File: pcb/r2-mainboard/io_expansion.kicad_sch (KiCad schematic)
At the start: 16 parts, among them J22 HC-FPC-05-09-6RLTAG, J23 HC-FPC-05-09-6RLTAG, J28 USB-C 16P, U54 TPS22914BYFPR, U55 TPS22914BYFPR, U56 TPS2553DBVR, U57 USBLC6-2SC6

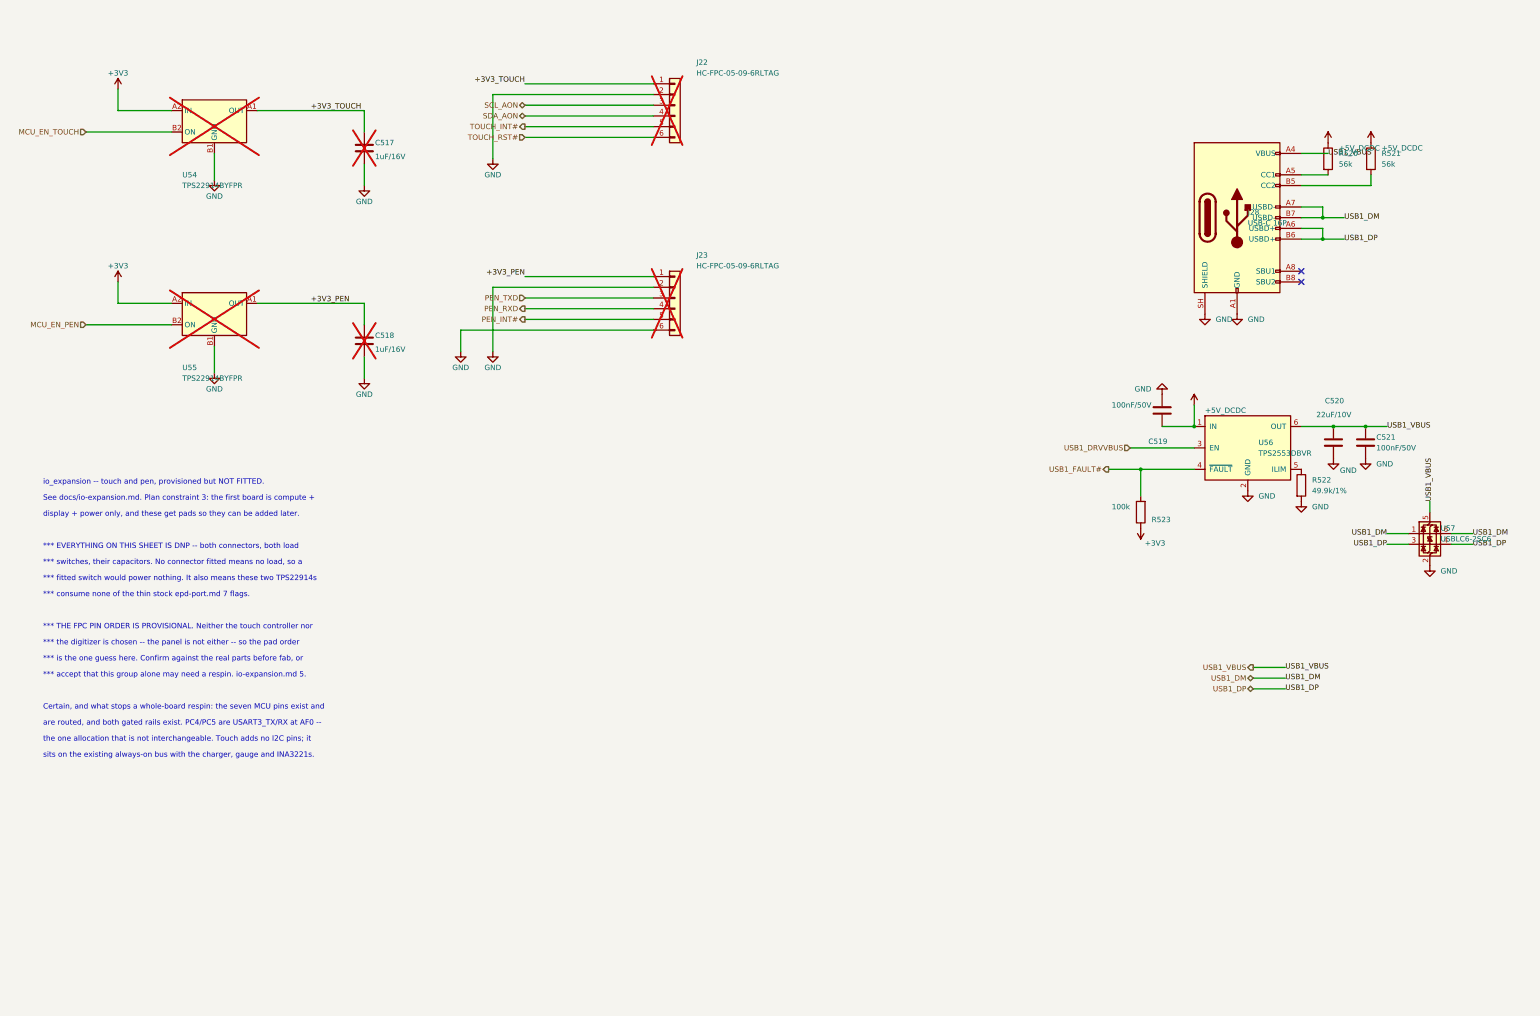
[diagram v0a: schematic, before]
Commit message: Touch decided: I2C hand-wired for the prototype; Caster bitgen applied
Good Display's answer of 2026-08-31 closes the on-board GT9110H idea:
the driving board is another customer's design and they will not share
files, so the panel's ITO channel map is unobtainable at prototype
scale. The production path is now priced instead -- US$750 tooling,
MOQ 1000/lot, for a custom panel with the interface and touch IC of our
choosing.

Owner's decision: option C. Touch runs over I2C on J22, hand-wired to
the vendor board's test points for the prototype. USB was rejected --
USB0 is the charge port and USB1 is now the host port, so USB touch
would have needed a hub and would have cost touch-to-wake permanently.
No schematic change: J22/J23 and U54/U55 stay exactly as drawn, DNP.

io-expansion.md 5.2 records the decision and the three firmware ways to
disable touch-to-wake; 5.3 records a real gap found on the vendor board
-- it exposes SDA/SCL/VDD/GND/DBG/INT/DP and *no* RST pad, so reset
becomes a power cycle through MCU_EN_TOUCH, and the GT9110's I2C
address cannot be selected and must be scanned for at bring-up.

Also in this commit, the owner's work: Caster bitgen at ConfigRate 22 /
x4 / binary (submodule pointer bump), epd_power and io_expansion sheet
edits, and board layout.

Co-Authored-By: Claude Opus 5 <noreply@anthropic.com>
Claude-Session: https://claude.ai/code/session_01MHTAe6ZnhogTEgtyPcLhwG
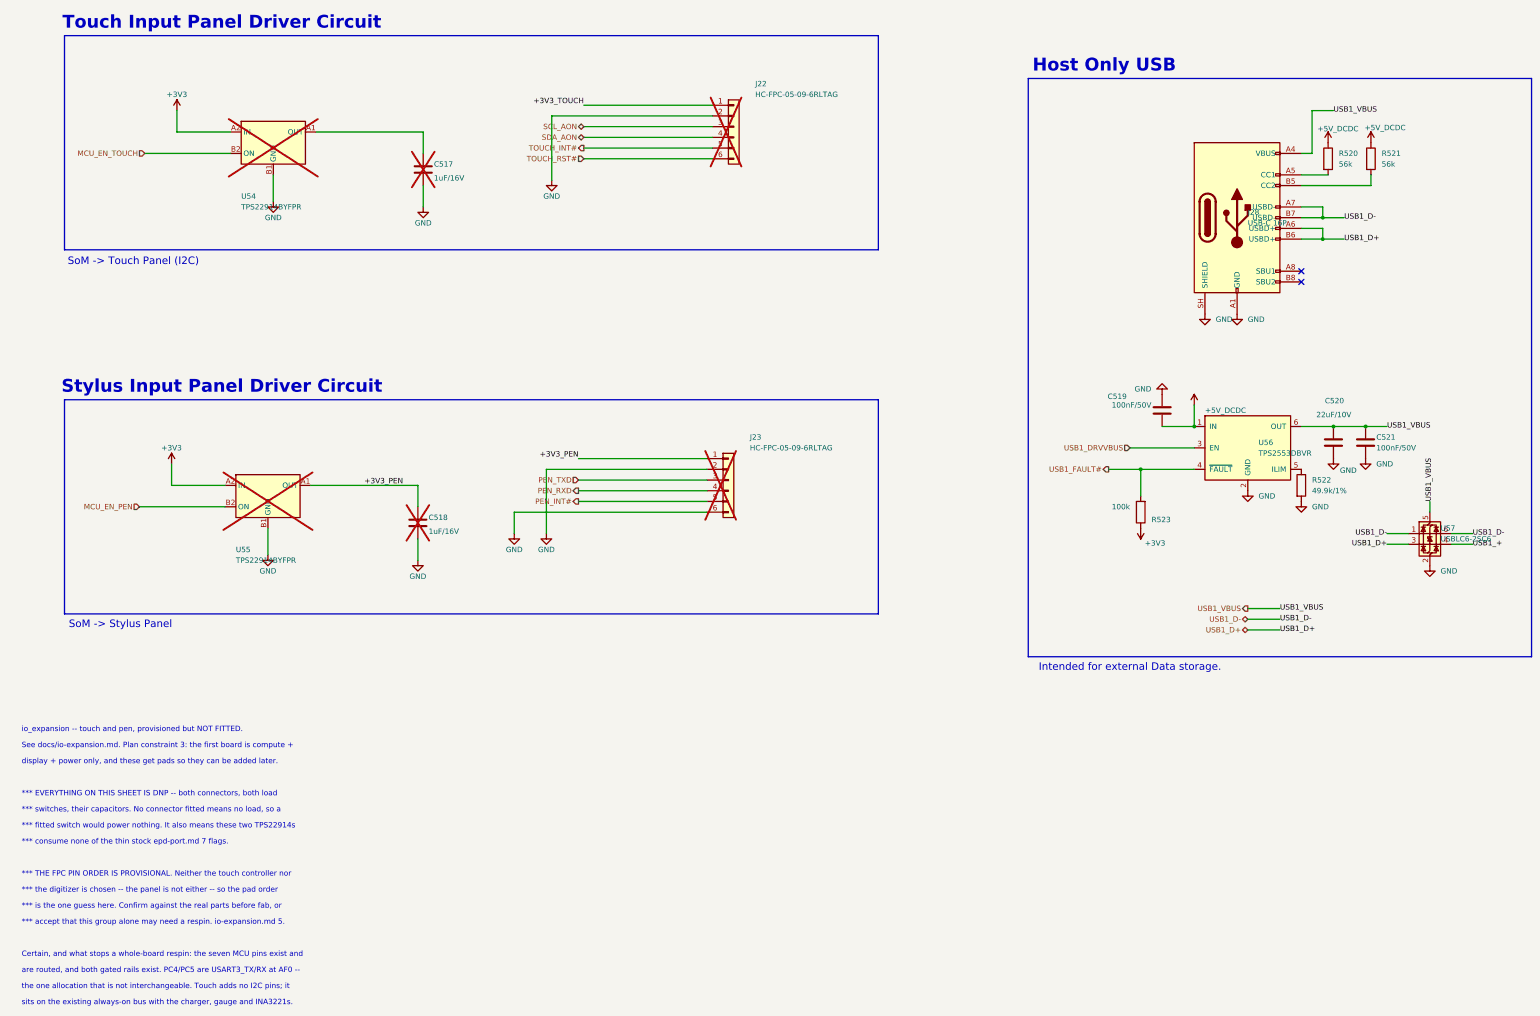
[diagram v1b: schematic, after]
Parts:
- C518, J23, U55: now left out of the parts list
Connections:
- net +3V3_TOUCH: no longer C517.1, U54.A1 (OUT)
- net USB1_DM renamed USB1_D-
- net USB1_DP renamed USB1_D+
- net USB1_D+: no longer U57.4 (I/O2)
- new net: C517.1, U54.A1 (OUT)
- new net USB1_+: U57.4 (I/O2)
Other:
- note added: "Host Only USB"
- note added: "Intended for external Data storage."
- note added: "SoM -> Stylus Panel"
- note added: "SoM -> Touch Panel (I2C)"
- note added: "Stylus Input Panel Driver Circuit"
- note added: "Touch Input Panel Driver Circuit"
- moved on the sheet: C517, C518, J22, J23, U54, U55

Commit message: Docs: library audit list and a first production costing
libraries.md -- every symbol in r2.kicad_sym and every footprint in
r2.pretty, with what it was derived from, which tools/ script emits it,
and what was actually checked. Written for the owner's audit before the
libraries get rehomed. Notes that pcb_common has never been modified,
and calls out the three newest entries (TPS2553DBV and the two
_Mirrored FPC land patterns) as the least reviewed.

NOTES-production-costing.md -- what 1000 units costs and what a campaign
would have to raise, prompted by Good Display's US$750 / MOQ 1000 quote.
Central estimate EUR 340/unit COGS and a EUR ~548k goal, but the honest
finding is the sensitivity: the PCM-071 at EUR 250 @1-9 costs more than
the display, and the sibling quote says ~EUR 190 of that is a memory-
shortage surcharge. A 1000-piece quote moves the goal by EUR 290k, so it
is the single highest-value thing to chase. Also states plainly that at
the central estimate the margin is thin to negative against market
comparables, and what to do about it.

Both indexed in CLAUDE.md.

Co-Authored-By: Claude Opus 5 <noreply@anthropic.com>
Claude-Session: https://claude.ai/code/session_01MHTAe6ZnhogTEgtyPcLhwG
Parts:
- C517, J22, U54: now fitted
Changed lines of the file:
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@@
 	(wire
 		(pts
-			(xy 69.85 73.66) (xy 49.53 73.66)
+			(xy 69.85 73.66) (xy 54.61 73.66)
 		)
 		(stroke
@@
 	(wire
 		(pts
-			(xy 146.05 64.77) (xy 146.05 80.01)
+			(xy 137.16 64.77) (xy 137.16 77.47)
 		)
 		(stroke
@@
 	(wire
 		(pts
-			(xy 184.15 64.77) (xy 146.05 64.77)
+			(xy 184.15 64.77) (xy 137.16 64.77)
 		)
 		(stroke
@@
 	(hierarchical_label "MCU_EN_TOUCH"
 		(shape input)
-		(at 49.53 73.66 180)
+		(at 54.61 73.66 180)
 		(effects
 			(font
@@
 	(symbol
 		(lib_id "power:GND")
-		(at 146.05 80.01 0)
+		(at 137.16 77.47 0)
 		(unit 1)
 		(body_style 1)
@@
 		(dnp no)
 		(property "Reference" "#PWR1107"
-			(at 146.05 80.01 0)
+			(at 137.16 77.47 0)
 			(hide yes)
 			(show_name no)
@@
 		)
 		(property "Value" "GND"
-			(at 146.05 83.82 0)
+			(at 137.16 81.28 0)
 			(show_name no)
 			(do_not_autoplace no)
@@
 		)
 		(property "Footprint" ""
-			(at 146.05 80.01 0)
+			(at 137.16 77.47 0)
 			(hide yes)
 			(show_name no)
@@
 		)
 		(property "Datasheet" ""
-			(at 146.05 80.01 0)
+			(at 137.16 77.47 0)
 			(hide yes)
 			(show_name no)
@@
 		)
 		(property "Description" ""
-			(at 146.05 80.01 0)
+			(at 137.16 77.47 0)
 			(hide yes)
 			(show_name no)
@@
 		(on_board yes)
 		(in_pos_files yes)
-		(dnp yes)
+		(dnp no)
 		(property "Reference" "C517"
 			(at 118.11 76.2 0)
@@
 		(on_board yes)
 		(in_pos_files yes)
-		(dnp yes)
+		(dnp no)
 		(property "Reference" "J22"
 			(at 194.31 57.15 0)
@@
 		(on_board yes)
 		(in_pos_files yes)
-		(dnp yes)
+		(dnp no)
 		(property "Reference" "U54"
-			(at 72.39 83.82 0)
+			(at 77.724 61.976 0)
 			(show_name no)
 			(do_not_autoplace no)
@@
 		)
 		(property "Value" "TPS22914BYFPR"
-			(at 72.39 86.36 0)
-			(show_name no)
-			(do_not_autoplace no)
+			(at 77.724 64.516 0)
+			(show_name no)
+			(do_not_autoplace no)

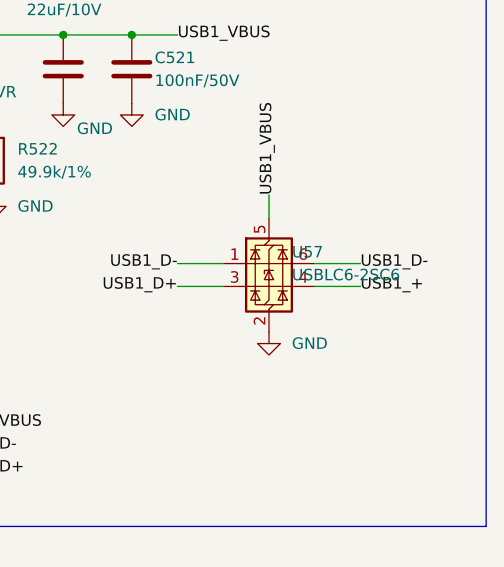
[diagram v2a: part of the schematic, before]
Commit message: Recover from the KiCad crash; finish the USB1_D+/D- rename
KiCad crashed and deleted 150 tracked files plus 19 untracked ones.
Recovery, in the order that matters:

  1. copied _restore_backup_2026-08-31T20-57-08-688 aside (261 MB)
  2. rescued the 4 untracked files that existed only there -- the
     PHYTEC PCM-071 STEP/x_t/Basic models and the library/3dmodels copy.
     The other 15 were __pycache__, .lck and .bak.
  3. git checkout of the 150 deletions (deletions only, so the six
     modified files were never touched)
  4. three files the crash had *rolled back* rather than deleted, and
     which git checkout therefore missed, restored from HEAD:
       r2.kicad_sym    -- was 11 symbols, missing TPS2553DBV,
                          BTH-060_AB/CD and BOM_ITEM, and carrying the
                          superseded PCM-071 symbol: the pre-2026-08-20
                          state, before the SoM was split in two
       sym-lib-table   -- had lost the Reflow declaration
       fp-lib-table    -- had lost Reflow and (version 7)

r2.kicad_pcb was not damaged -- 328 footprints, 471 segments, same as
HEAD. Rescuing PCM-071_1573-1.STEP also repairs X2's 3D model path,
which an earlier restore had broken.

Separately, the USB1 net rename is finished at the owner's request:
som.kicad_sch USB1_DM/DP -> USB1_D-/D+ (the J26 X_USB1_* pin names are
PHYTEC's and are untouched), and a USB1_+ typo on U57's second ESD stub
in io_expansion corrected to USB1_D+. sheet_pins + wire_root re-run:
113 names on 233 sheet pins, 113 joined, 0 one-sided. All five USB1
nets verified node-for-node.

⚠ The tree is mid-renumber (J200/U200/U300... appearing) and carries one
severed net: +3V3_TOUCH reaches only J22.1, while U54.A1 and C517.1 sit
on an unnamed Net-(U54-OUT). Committed as-is so the recovery is not at
risk from another crash; the break is called out rather than hidden.

Co-Authored-By: Claude Opus 5 <noreply@anthropic.com>
Claude-Session: https://claude.ai/code/session_01MHTAe6Znh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
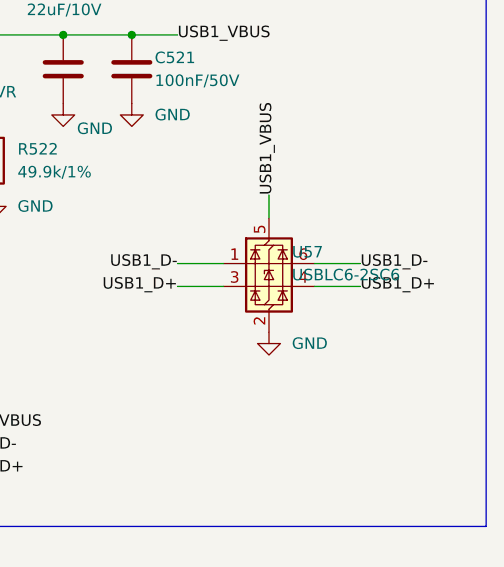
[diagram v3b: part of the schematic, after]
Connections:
- net USB1_+ is gone; now on net USB1_D+: U57.4 (I/O2)
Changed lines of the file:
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@@
 		)
 	)
-	(label "USB1_+"
+	(label "USB1_D+"
 		(at 364.49 166.37 0)
 		(effects

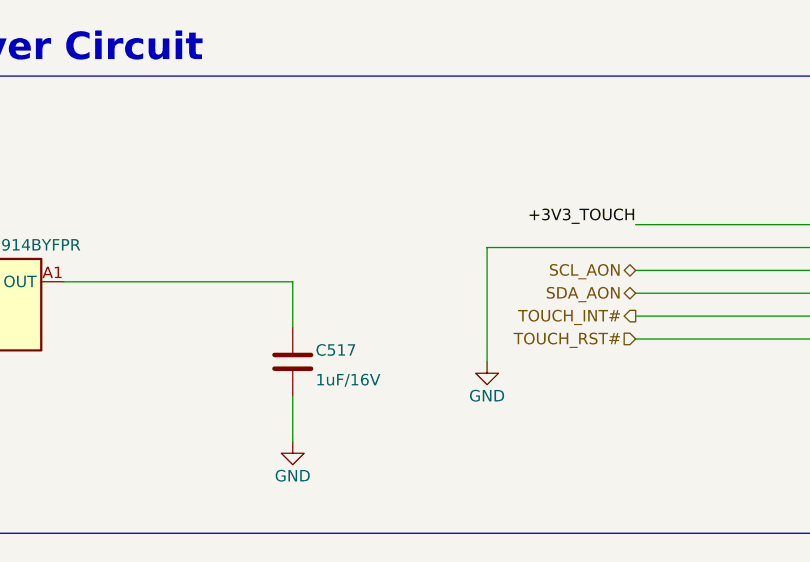
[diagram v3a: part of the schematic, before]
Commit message: Fix the severed +3V3_TOUCH rail and U902's GND pin type
+3V3_TOUCH reached only J22.1; U54.A1 and C517.1 sat on an unnamed
Net-(U54-OUT) after the io_expansion re-layout. Added a stub and label on
the switch output at (115.57..127, 68.58). The rail is now
U54.A1 + C517.1 + J22.1 as intended.

U902's GND (pin 4) was typed power_out in Reflow:WSON_Flash -- a flash's
ground is a consumer. That one wrong type produced both pin_to_pin
errors, conflicting with the GND PWR_FLAG and with U41.N11's M1 strap.
Changed to power_in, and EP (pin 9) from power_out to passive. Patched in
both the library and the copy fpga_config.kicad_sch embeds, since the
schematic uses the embedded one.

ERC: 14 errors / 20 warnings -- the pre-crash baseline. pin_to_pin is
back to the single documented U41.N11 warning (fpga.md 4.1), and
isolated_pin_label and hier_label_mismatch are gone.

Not a defect, for the record: U55/C518/J23 (pen) are absent from the
netlist because they carry on_board=no, in_bom=no -- deliberately
excluded, unlike the touch group which is now dnp=no and fitted.

⚠ The library symbol has a pin 9 (EP) that the embedded copy does not,
and the SOIC-8 footprint has no ninth pad. Worth reconciling.

Co-Authored-By: Claude Opus 5 <noreply@anthropic.com>
Claude-Session: https://claude.ai/code/session_01MHTAe6ZnhogTEgtyPcLhwG
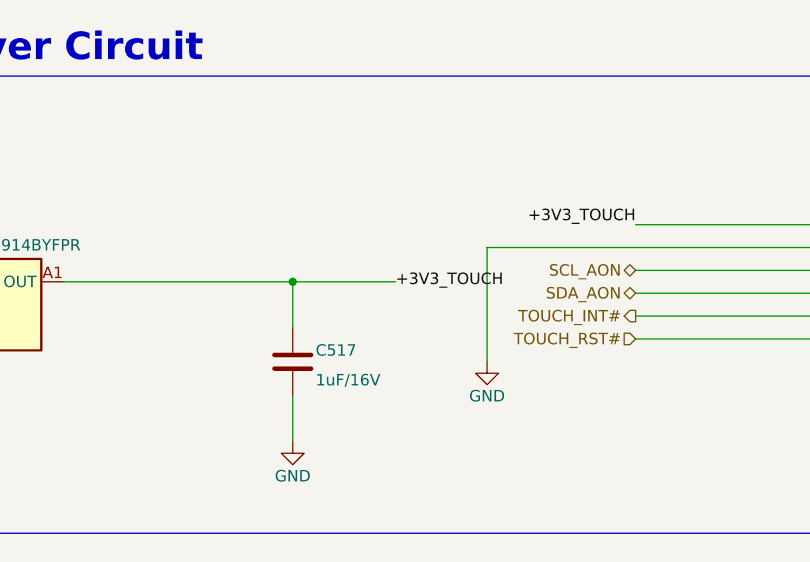
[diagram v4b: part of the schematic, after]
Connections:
- net +3V3_TOUCH: now also C517.1, U54.A1 (OUT)
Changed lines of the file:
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@@
+		)
+	)
+	(wire
+		(pts
+			(xy 115.57 68.58) (xy 127 68.58)
+		)
+		(stroke
+			(width 0)
+			(type default)
+		)
+	)
+	(junction
+		(at 115.57 68.58)
+		(diameter 0)
+		(color 0 0 0 0)
+	)
+	(label "+3V3_TOUCH"
+		(at 127 68.58 0)
+		(effects
+			(font
+				(size 1.27 1.27)
+			)
+			(justify left)
 		)
 	)
